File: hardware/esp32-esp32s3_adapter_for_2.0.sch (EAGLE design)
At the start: 3 parts, among them U1 ESP32-S3-WROOM-1-N16R2, U2 ESP32-WROOM-32E_(16MB)

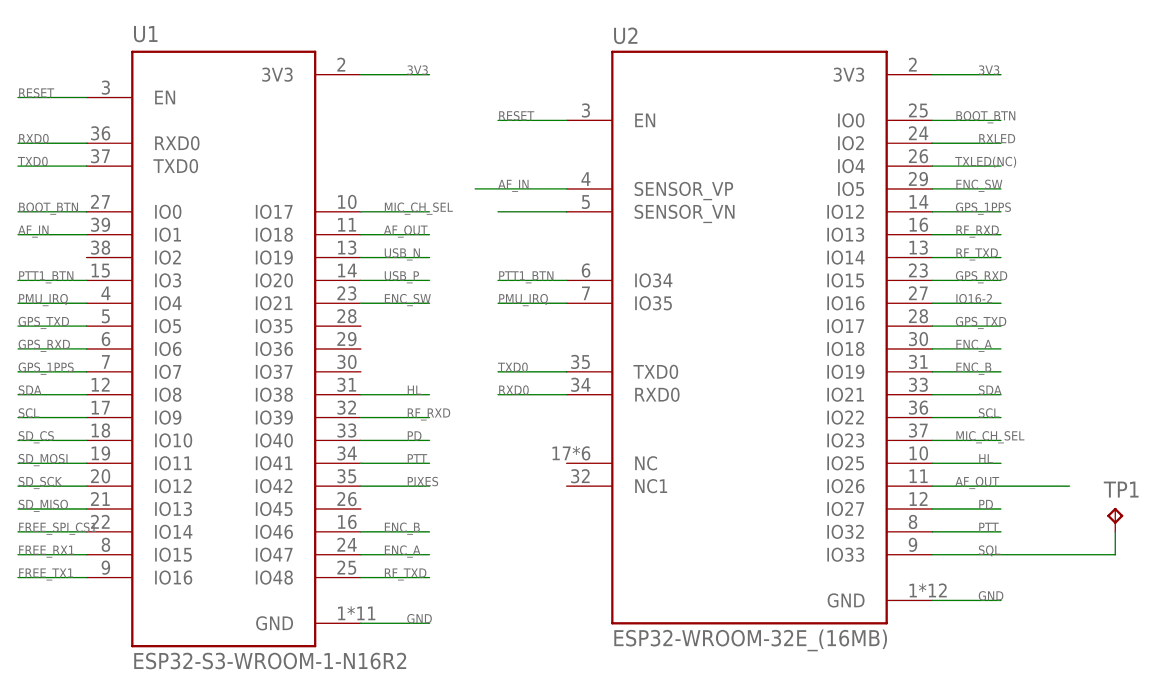
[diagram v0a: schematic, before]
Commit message: Added RevB of ESP32toESP32S3 V1.4 and 2.0
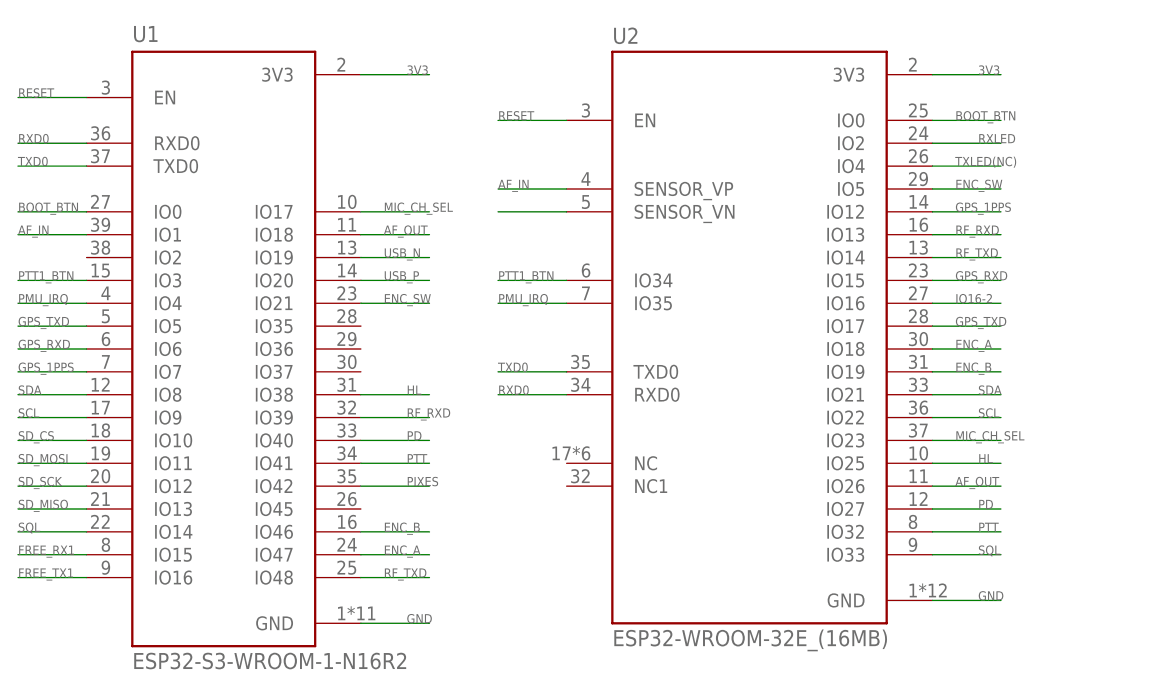
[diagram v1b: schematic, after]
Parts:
- removed TP1: TPB1,27, testpad:TPB1,27
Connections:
- removed net FREE_SPI_CS1: U1.IO14
- net SQL: now also U1.IO14; no longer TP1.TP
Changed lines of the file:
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@@
 <part name="U1" library="ESP32-S3-WROOM-1-N16R2" deviceset="ESP32-S3-WROOM-1-N16R2" device=""/>
 <part name="U2" library="ESP32-WROOM-32E__16MB_" deviceset="ESP32-WROOM-32E_(16MB)" device=""/>
-<part name="TP1" library="testpad" library_urn="urn:adsk.eagle:library:385" deviceset="TP" device="B1,27" package3d_urn="urn:adsk.eagle:package:27944/2"/>
 </parts>
 <sheets>
@@
 <attribute name="VALUE" x="68.58" y="15.24" size="1.778" layer="96"/>
 </instance>
-<instance part="TP1" gate="G$1" x="124.46" y="30.48" smashed="yes">
-<attribute name="NAME" x="123.19" y="31.75" size="1.778" layer="95"/>
-<attribute name="TP_SIGNAL_NAME" x="125.73" y="29.21" size="1.778" layer="97"/>
-</instance>
 </instances>
 <busses>
@@
 <segment>
 <pinref part="U2" gate="G$1" pin="SENSOR_VP"/>
-<wire x1="63.5" y1="66.04" x2="53.34" y2="66.04" width="0.1524" layer="91"/>
+<wire x1="63.5" y1="66.04" x2="55.88" y2="66.04" width="0.1524" layer="91"/>
 <label x="55.88" y="66.04" size="1.016" layer="95"/>
 </segment>
@@
 <pinref part="U2" gate="G$1" pin="IO26"/>
 <label x="106.68" y="33.02" size="1.016" layer="95"/>
-<wire x1="119.38" y1="33.02" x2="104.14" y2="33.02" width="0.1524" layer="91"/>
+<wire x1="111.76" y1="33.02" x2="104.14" y2="33.02" width="0.1524" layer="91"/>
 </segment>
 <segment>
@@
 <pinref part="U2" gate="G$1" pin="IO33"/>
 <label x="109.22" y="25.4" size="1.016" layer="95"/>
-<wire x1="104.14" y1="25.4" x2="124.46" y2="25.4" width="0.1524" layer="91"/>
-<pinref part="TP1" gate="G$1" pin="TP"/>
-<wire x1="124.46" y1="27.94" x2="124.46" y2="25.4" width="0.1524" layer="91"/>
-</segment>
-</net>
-<net name="FREE_SPI_CS1" class="0">
+<wire x1="104.14" y1="25.4" x2="111.76" y2="25.4" width="0.1524" layer="91"/>
+</segment>
 <segment>
 <pinref part="U1" gate="G$1" pin="IO14"/>
@@
 </schematic>
 </drawing>
-<compatibility>
-<note version="8.2" severity="warning">
-Since Version 8.2, EAGLE supports online libraries. The ids
-of those online libraries will not be understood (or retained)
-with this version.
-</note>
-<note version="8.3" severity="warning">
-Since Version 8.3, EAGLE supports URNs for individual library
-assets (packages, symbols, and devices). The URNs of those assets
-will not be understood (or retained) with this version.
-</note>
-<note version="8.3" severity="warning">
-Since Version 8.3, EAGLE supports the association of 3D packages
-with devices in libraries, schematics, and board files. Those 3D
-packages will not be understood (or retained) with this version.
-</note>
-</compatibility>
 </eagle>

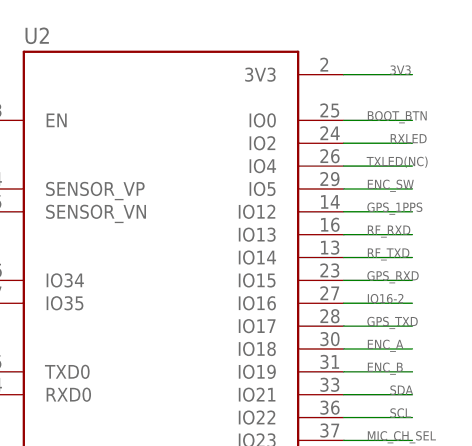
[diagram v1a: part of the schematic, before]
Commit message: - T-TWR PLUS V2.0 MOD board support added
- ESP32S3 -> ESP32E adapter Rev.C added
- AudioAdapter BOM fix (4k7->33k)
- README.md updated
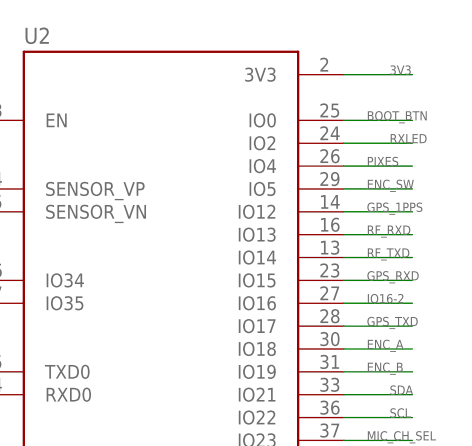
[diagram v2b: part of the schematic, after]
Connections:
- removed net TXLED(NC): U2.IO4
- net PIXES: now also U2.IO4
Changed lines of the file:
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@@
-</segment>
-</net>
-<net name="TXLED(NC)" class="0">
-<segment>
-<pinref part="U2" gate="G$1" pin="IO4"/>
-<wire x1="104.14" y1="68.58" x2="111.76" y2="68.58" width="0.1524" layer="91"/>
-<label x="106.68" y="68.58" size="1.016" layer="95"/>
 </segment>
 </net>
@@
 <label x="45.72" y="33.02" size="1.016" layer="95"/>
 </segment>
+<segment>
+<pinref part="U2" gate="G$1" pin="IO4"/>
+<wire x1="104.14" y1="68.58" x2="111.76" y2="68.58" width="0.1524" layer="91"/>
+<label x="106.68" y="68.58" size="1.016" layer="95"/>
+</segment>
 </net>
